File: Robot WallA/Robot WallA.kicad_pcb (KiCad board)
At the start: 4 copper layers, 170 x 100 mm, 315 parts, among them IC1 STM32F407IGT6, IC2 DS04-254-2-04BK-SMT, IC3 USBLC6-4SC6, IC4 USBLC6-4SC6, IC6 TLV75533PDBVR, IC7 ABXS005A4X341-SRZ, IC8 DRV8262DDVR, IC9 74LVC2G241DP-Q100H, J1 Conn_02x05_Female, J10 Conn_01x02, J11 Conn_01x02, J12 Conn_01x02, J13 10129383-916001ALF, J15 39501-1002, J16 39501-1002, J17 39501-1004, J18 39501-1004, J19 22-03-5035, J2 USB4216-03-A, J20 22-03-5035, J21 22-03-5035, J22 22-03-5035, J23 Conn_01x03, J24 281695-3, J25 Conn_01x03, J26 281695-3, J27 Conn_01x03, J28 281695-3, J29 Conn_01x03, J3 SS-90000-009, J30 39501-1002, J31 39501-1002, J32 Conn_01x03, J33 281695-3, J34 Conn_01x03, J35 SM04B-SRSS-TB, J36 SM04B-SRSS-TB, J37 SM04B-SRSS-TB, J38 SM02B-SRSS-TB_LF__SN_, J39 Conn_01x03, J4 USB_B_Micro, J40 SM03B-SRSS-TB_LF__SN_, J41 SM03B-SRSS-TB_LF__SN_, J42 SM03B-SRSS-TB_LF__SN_, J43 SM03B-SRSS-TB_LF__SN_, J44 SM02B-SRSS-TB_LF__SN_, J45 SM04B-SRSS-TB, J46 SM02B-SRSS-TB_LF__SN_, J47 SM02B-SRSS-TB_LF__SN_, J6 10129383-916001ALF, J7 Conn_01x02, J8 XT90PW_M, J9 Conn_01x02, Q1 BSS138, Q2 BSS138, Q3 BSS138, Q4 BSS119, Q5 BSS119, Q6 BSS138, SW1 Switch, T1 H1102NL, U1 FT231XS, U10 PTN78060W_EUW-7, U2 125700D00000G, U3 125700D00000G, U4 125700D00000G, U5 125700D00000G, U6 L298N, U7 LAN8742A, U8 PTN78020W, U9 PTN78060W_EUW-7, Y1 Crystal_GND24, Y2 Crystal_GND24

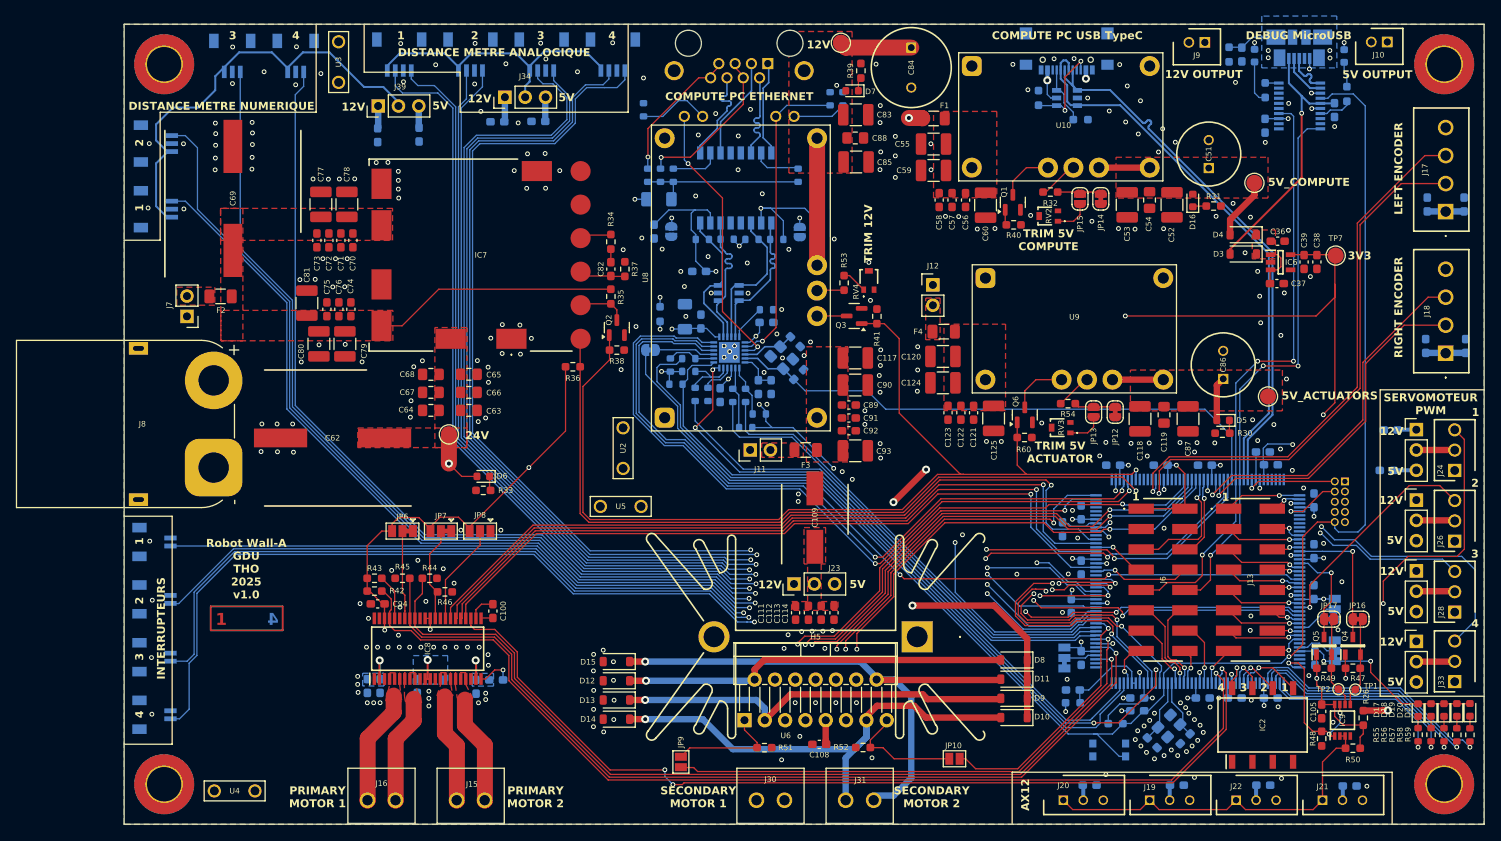
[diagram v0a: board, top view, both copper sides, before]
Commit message: Moved 24V boost to be correct assembly issue with heatsink fixation collisions
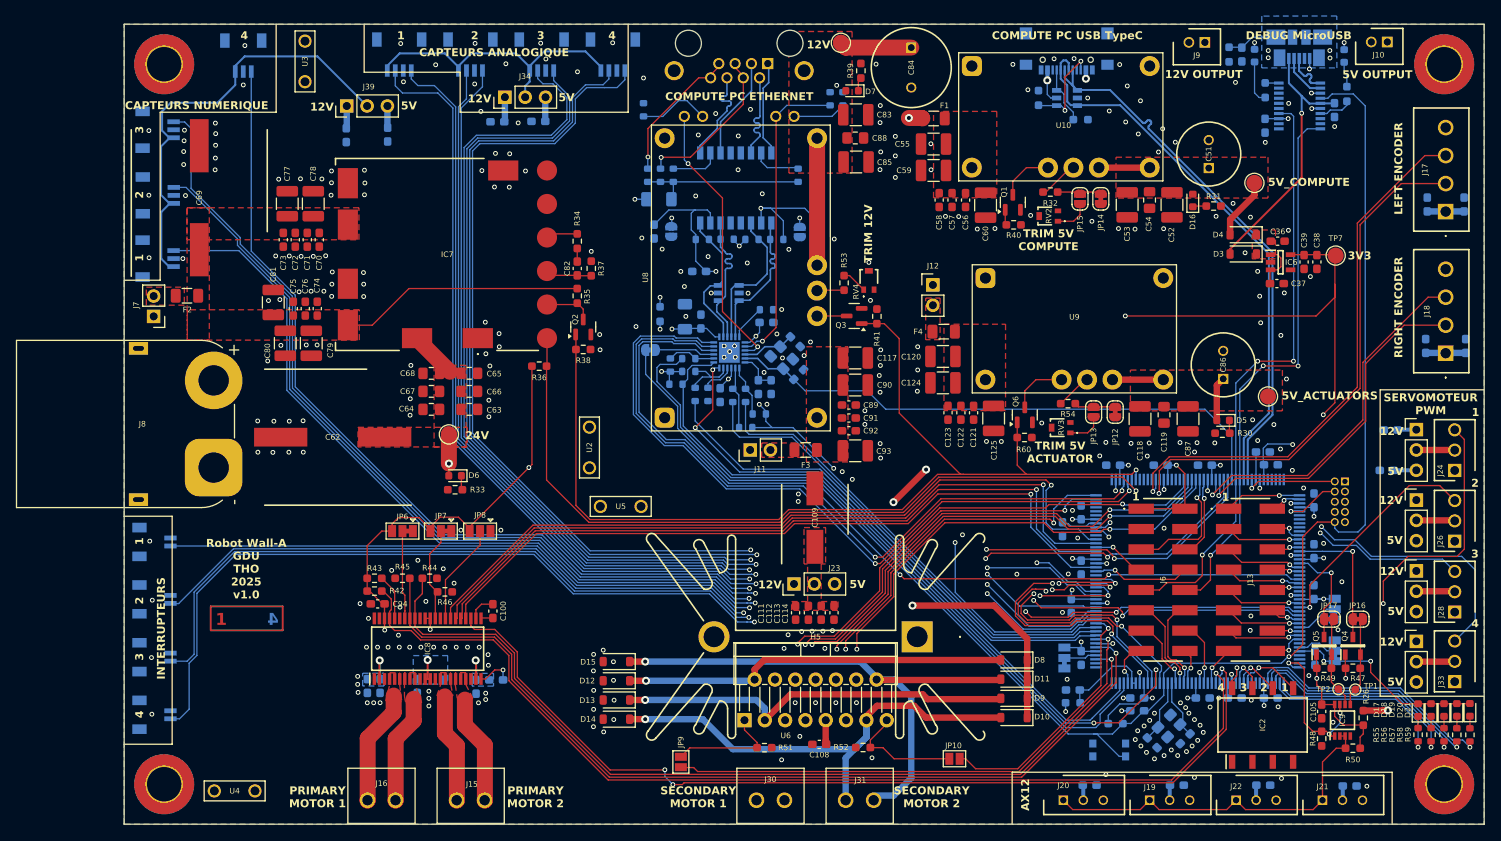
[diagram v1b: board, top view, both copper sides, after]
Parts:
- moved J41 13.8 mm to (58.9, 52.7), turned to 90 degrees
- moved J43 6.55 mm to (70.1, 42.9)
- moved J42 6.48 mm to (59.0, 60.9)
- moved J40 6.18 mm to (58.9, 68.8)
- moved C69 4.20 mm to (64.6, 61.2)
- moved C70 4.20 mm to (79.6, 66.4)
- moved C71 4.20 mm to (78.1, 66.4)
- moved C72 4.20 mm to (76.6, 66.4)
- moved C73 4.20 mm to (75.1, 66.4)
- moved C74 4.20 mm to (79.3, 75.0)
- moved C75 4.20 mm to (76.3, 75.0)
- moved C76 4.20 mm to (77.8, 75.0)
- moved C77 4.20 mm to (75.6, 61.9)
- moved C78 4.20 mm to (78.8, 61.9)
- moved C79 4.20 mm to (78.6, 79.4)
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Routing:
- net /MCU/SENSORS9: track 177.3 -> 168.7 mm
- net /MCU/SENSORS8: track 177.5 -> 173.0 mm
- net /Sensors/Vcc: track 52.5 -> 56.6 mm
- net /MCU/SENSORS10: track 188.0 -> 184.1 mm
- net /Motor/5V: track 403.4 -> 407.3 mm
- net /Power/12V: track 383.6 -> 387.4 mm
- net /Power/24V: track 65.9 -> 69.1 mm
- net /Power/Vbatt: track 133.2 -> 135.4 mm
- net /Power/GPIO_PGOOD: track 96.4 -> 98.3 mm
- net /MCU/3V3: track 466.4 -> 464.7 mm
- net /Power/GPIO_ENABLE_POWER_SUPPLIES: track 129.7 -> 128.8 mm
- net /Power/Power_Boost_24V/TRIM: track 4.94 -> 5.78 mm
- net /Power/Power_Boost_24V/SENSE+: track 3.33 -> 3.97 mm
- net GND: vias 322 -> 324
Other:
- board text added: "CAPTEURS ANALOGIQUE"
- board text added: "CAPTEURS NUMERIQUE"
- board text removed: "DISTANCE METRE ANALOGIQUE"
- board text removed: "DISTANCE METRE NUMERIQUE"

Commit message: Added diode for Type-C connector in case we accidentally power the board with this connector.
Updated fab files
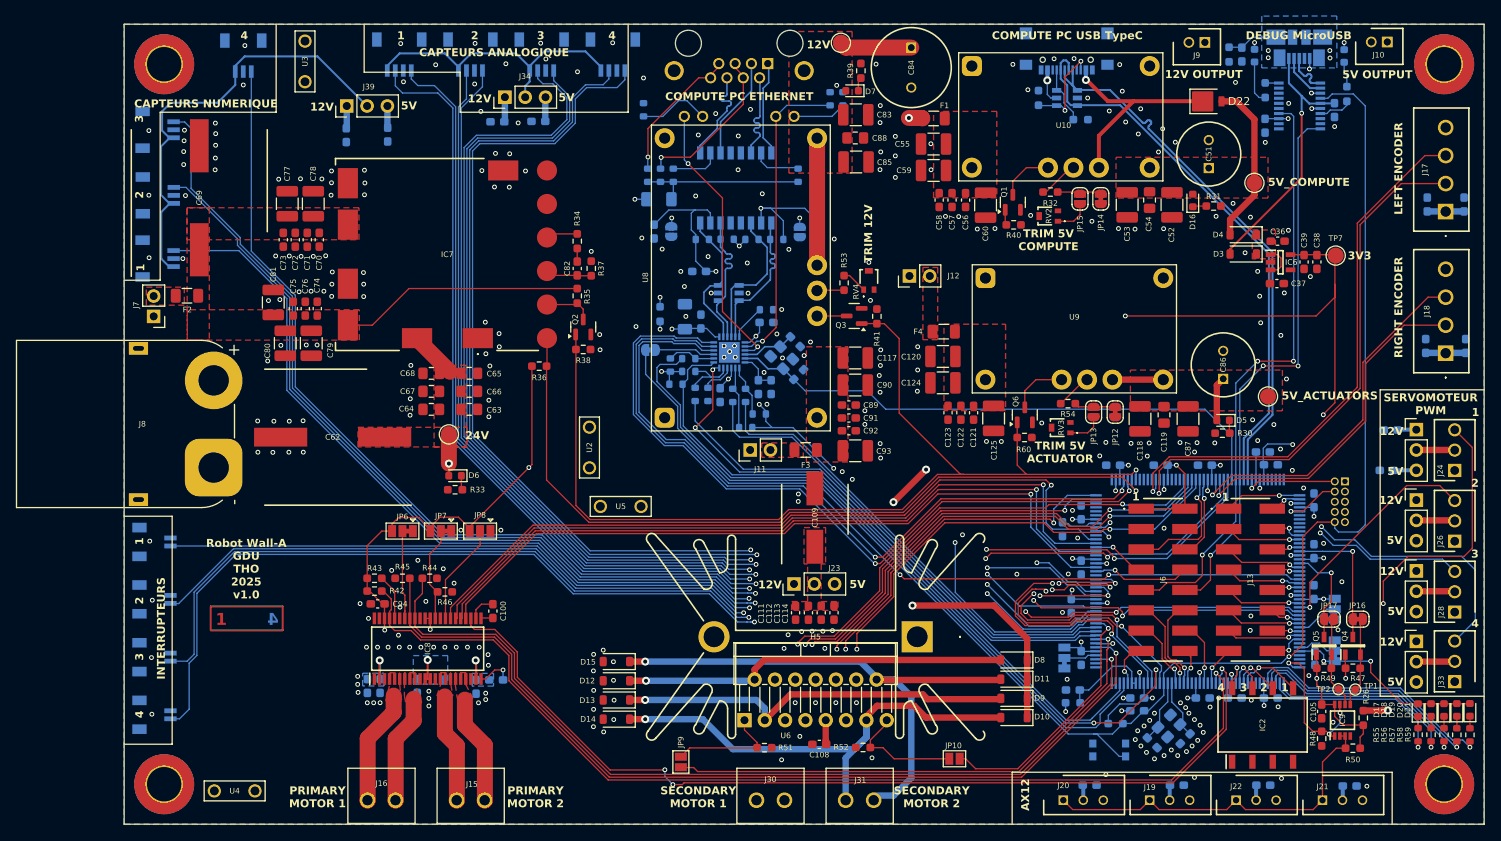
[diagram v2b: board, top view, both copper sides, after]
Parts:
- added D22: Diode 3A, Diode_SMD:D_SMP_DO-220AA, F.Cu at (190.7, 49.1)
- D17: value LED -> LED_YELLOW
- D18: value LED -> LED_ORANGE
- D19: value LED -> LED_GREEN
- D20: value LED -> LED_BLUE
- D21: value LED -> LED_RED
- moved J12 3.13 mm to (153.4, 71.0), turned to 90 degrees
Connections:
- IC3 pad 5: /MCU/5V_PC_EMBARQUE -> /MCU/MCU_Peripherals/5V_USB
- J2 pad A4: /MCU/5V_PC_EMBARQUE -> /MCU/MCU_Peripherals/5V_USB
- J2 pad B4: /MCU/5V_PC_EMBARQUE -> /MCU/MCU_Peripherals/5V_USB
- U10 pad 5: /MCU/5V_PC_EMBARQUE -> /MCU/MCU_Peripherals/5V_USB
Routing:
- net /MCU/MCU_Peripherals/5V_USB: track 0.00 -> 36.3 mm, vias 0 -> 2
- net /MCU/5V_PC_EMBARQUE: track 40.5 -> 20.7 mm, vias 2 -> 0
- net /Power/Vbatt: track 135.4 -> 132.4 mm
- net /MCU/SERVO3: track 68.2 -> 69.5 mm

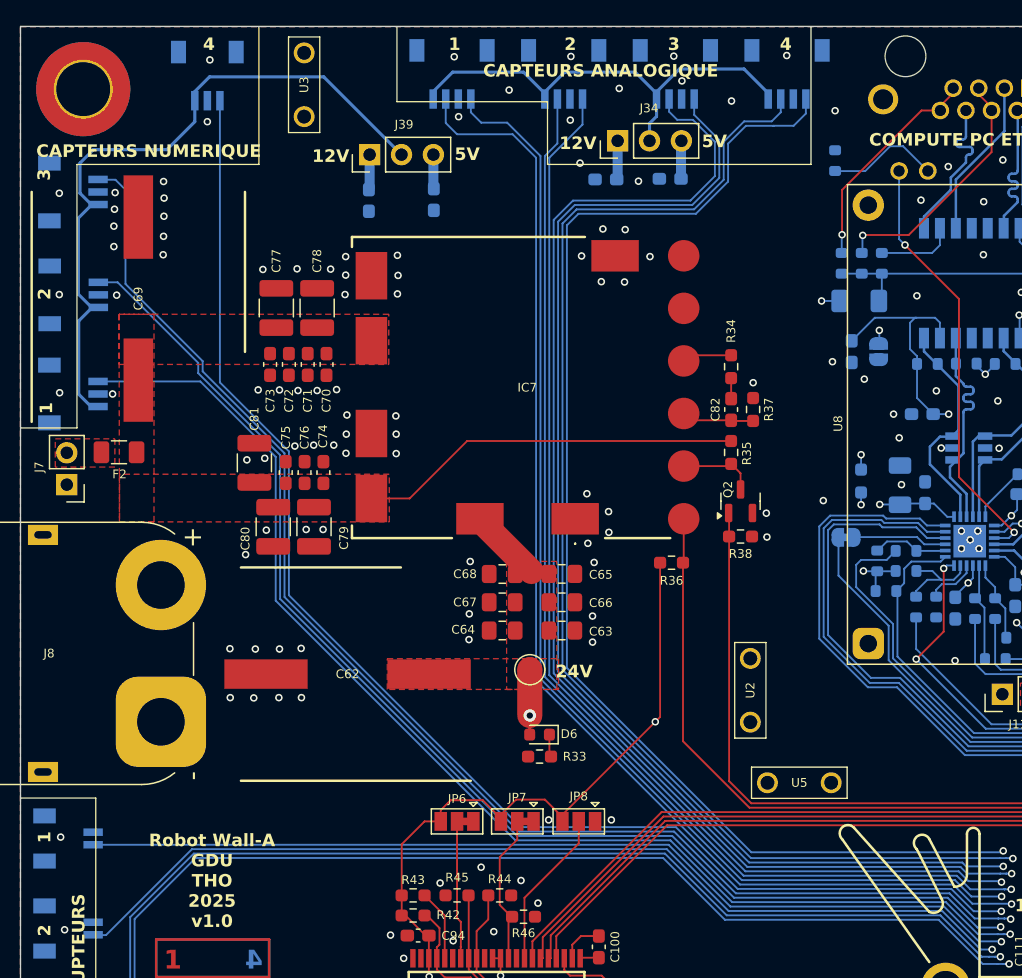
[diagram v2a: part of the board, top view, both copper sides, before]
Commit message: Added to BOM connectors and socket
Updated fab files
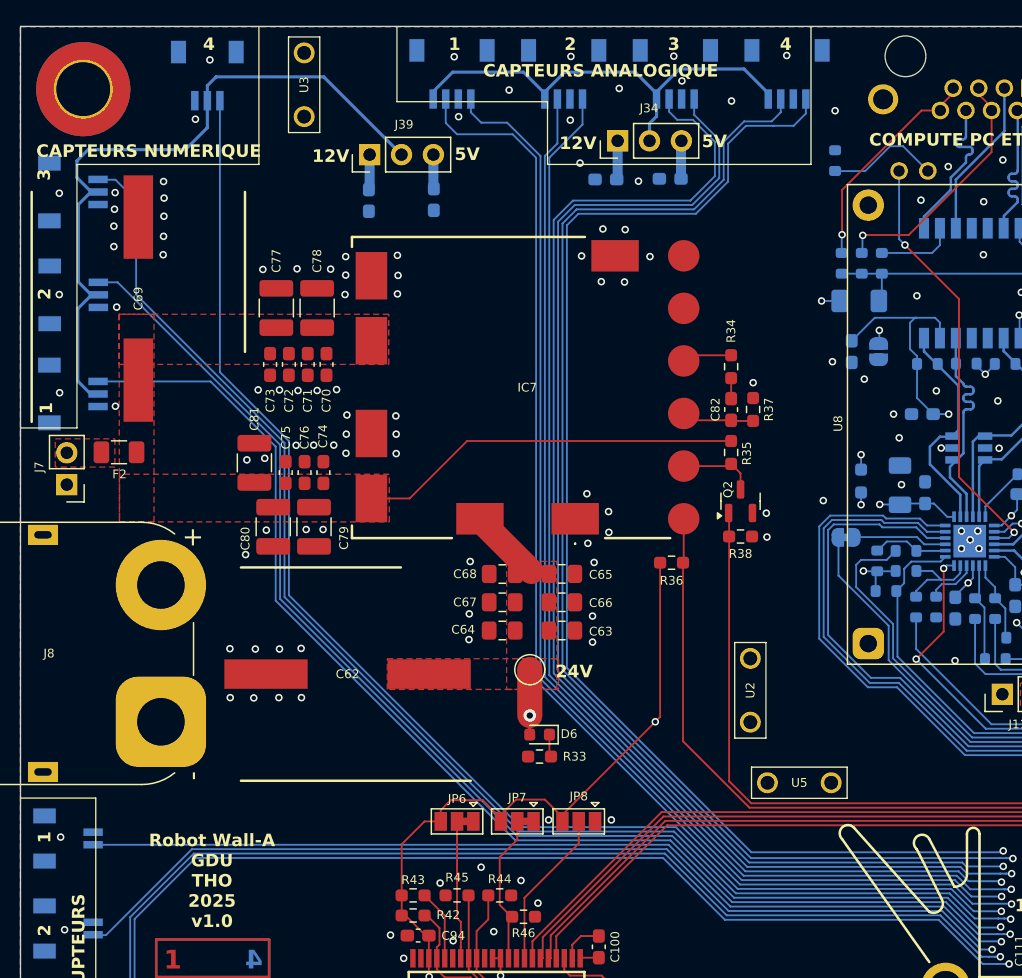
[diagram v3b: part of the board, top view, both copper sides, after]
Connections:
- J40 pad 1: /Sensors/Vcc -> GND
- J40 pad 2: GND -> /Sensors/Vcc
- J41 pad 1: /Sensors/Vcc -> GND
- J41 pad 2: GND -> /Sensors/Vcc
- J42 pad 1: /Sensors/Vcc -> GND
- J42 pad 2: GND -> /Sensors/Vcc
- J43 pad 1: /Sensors/Vcc -> GND
- J43 pad 2: GND -> /Sensors/Vcc
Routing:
- net GND: track 19.7 -> 22.4 mm
